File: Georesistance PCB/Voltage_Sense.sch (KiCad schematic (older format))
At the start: 26 parts, among them Q1 MMBF4117, Q2 MMBF4117, Q3 MMBF4117, Q4 MMBF4117, U1 RS8554, U2 LTC6915HGN-TRPBF, U3 LM4040DBZ-2.5

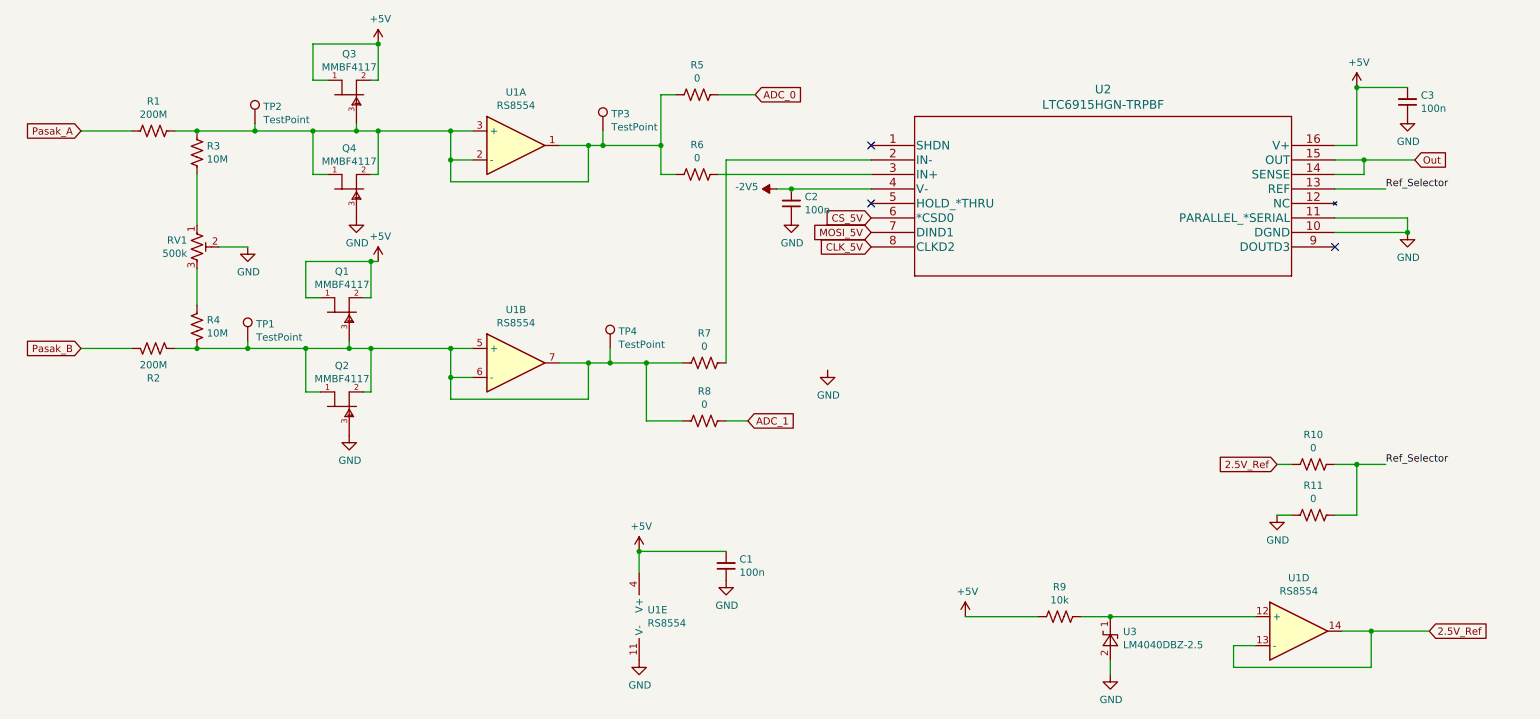
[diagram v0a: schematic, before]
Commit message: Added the PCB layout and simplified schematic
deleted jumper, and fixed misconnection
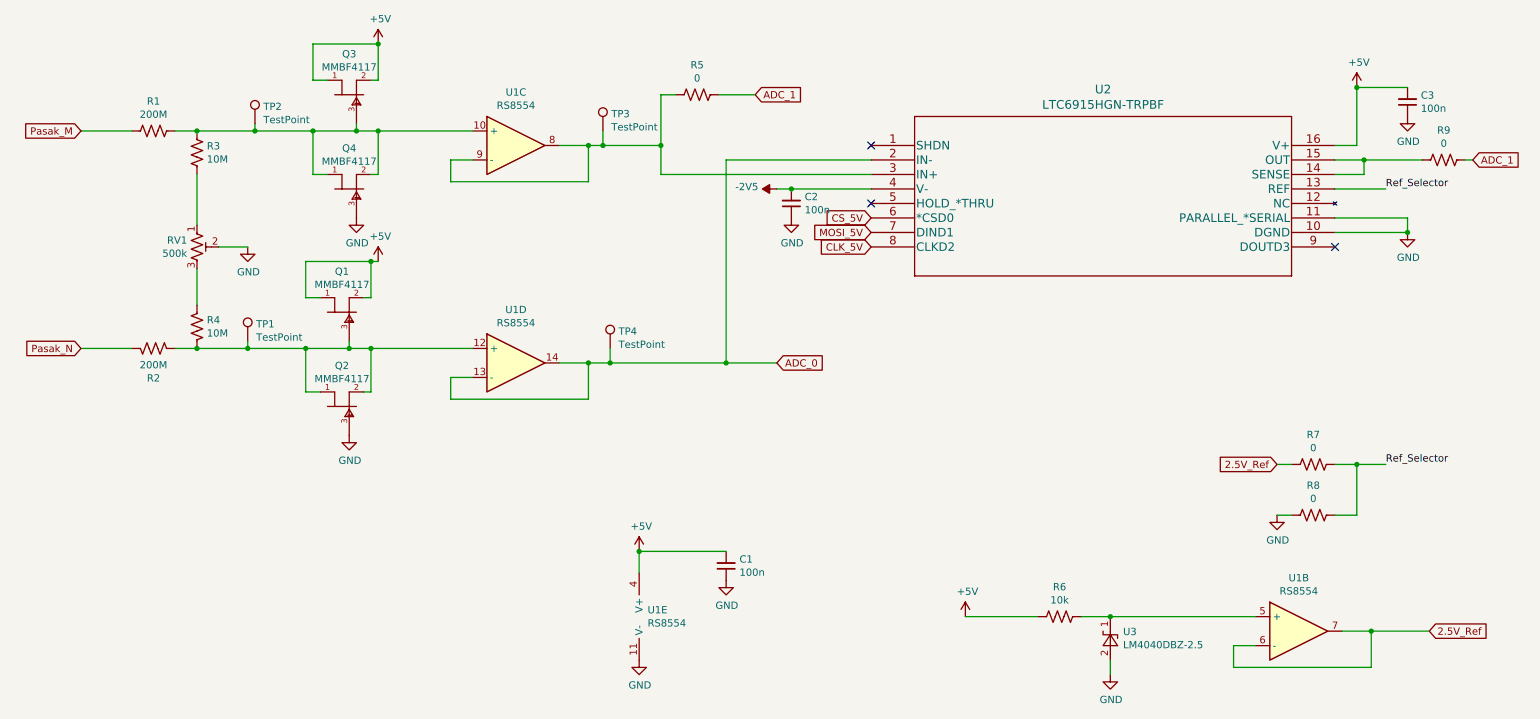
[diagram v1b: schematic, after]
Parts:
- removed R6, R7, R8: 0, Resistor_SMD:R_0402_1005Metric_Pad0.72x0.64mm_HandSolder, symbol Device:R_US
- added R9: 0, Resistor_SMD:R_0402_1005Metric_Pad0.72x0.64mm_HandSolder, symbol Device:R_US
- TP1, TP2, TP3, TP4: footprint TestPoint:TestPoint_Loop_D2.54mm_Drill1.5mm_Beaded -> TestPoint:TestPoint_THTPad_D1.0mm_Drill0.5mm
- renumbered R9 to R6, R10 to R7, R11 to R8
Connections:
- net 2.5V_Ref: now also U1.6 (-), U1.7; no longer U1.13 (-), U1.14
- net ADC_0: now also TP4.1, U1.13 (-), U1.14, U2.2 (IN-); no longer R5.1
- net ADC_1: now also R5.1, R9.1
- net at Q3.3 (G), Q4.1 (D), Q4.2 (S)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: now also U1.10 (+); no longer R5.2, TP3.1, U1.1, U1.2 (-), U1.3 (+)
- net at Q1.3 (G), Q2.1 (D), Q2.2 (S)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: now also U1.12 (+); no longer TP4.1, U1.5 (+), U1.6 (-), U1.7
- net at U2.3 (IN+): now also R5.2, TP3.1, U1.8, U1.9 (-)
- net at R6.1, U3.1 (K): now also U1.5 (+); no longer U1.12 (+)
- net Out: no longer names the net of U2.14 (SENSE), U2.15 (OUT)
- net Out: now also R9.2
- net Pasak_A renamed Pasak_M
- net Pasak_B renamed Pasak_N
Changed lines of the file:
@@
 F 0 "TP2" H 2458 2018 50  0000 L CNN
 F 1 "TestPoint" H 2458 1927 50  0000 L CNN
-F 2 "TestPoint:TestPoint_Loop_D2.54mm_Drill1.5mm_Beaded" H 2600 1900 50  0001 C CNN
+F 2 "TestPoint:TestPoint_THTPad_D1.0mm_Drill0.5mm" H 2600 1900 50  0001 C CNN
 F 3 "~" H 2600 1900 50  0001 C CNN
 	1    2400 1900
@@
 F 0 "TP1" H 2408 3518 50  0000 L CNN
 F 1 "TestPoint" H 2408 3427 50  0000 L CNN
-F 2 "TestPoint:TestPoint_Loop_D2.54mm_Drill1.5mm_Beaded" H 2550 3400 50  0001 C CNN
+F 2 "TestPoint:TestPoint_THTPad_D1.0mm_Drill0.5mm" H 2550 3400 50  0001 C CNN
 F 3 "~" H 2550 3400 50  0001 C CNN
 	1    2350 3400
@@
 	4700 2050 4700 2300
 Connection ~ 3250 1950
-Connection ~ 3750 2150
 Wire Wire Line
 	3750 2300 3750 2150
@@
 	4700 2300 3750 2300
 Wire Wire Line
-	3750 1950 3250 1950
-Connection ~ 3750 1950
-Wire Wire Line
 	3750 2150 3900 2150
 Wire Wire Line
-	3750 1950 3750 2150
-Wire Wire Line
-	3900 1950 3750 1950
-$Comp
-L Device:Opamp_Quad_Generic U1
-U 1 1 613E6A3C
-P 4200 2050
-F 0 "U1" H 4200 2417 50  0000 C CNN
-F 1 "RS8554" H 4200 2326 50  0000 C CNN
-F 2 "Package_SO:SOIC-14_3.9x8.7mm_P1.27mm" H 4200 2050 50  0001 C CNN
-F 3 "~" H 4200 2050 50  0001 C CNN
-	1    4200 2050
-	1    0    0    -1
-$EndComp
-Wire Wire Line
 	4700 3550 4700 3800
-Connection ~ 3750 3650
 Wire Wire Line
 	4500 3550 4700 3550
@@
 Wire Wire Line
 	4700 3800 3750 3800
-Connection ~ 3750 3450
 Wire Wire Line
 	3750 3650 3900 3650
-Wire Wire Line
-	3750 3450 3750 3650
-Wire Wire Line
-	3900 3450 3750 3450
-Wire Wire Line
-	3200 3450 3750 3450
 Connection ~ 3200 3450
 Wire Wire Line
@@
 	1550 1950 1200 1950
 Text GLabel 1200 1950 0    50   Input ~ 0
-Pasak_A
+Pasak_M
 Text GLabel 1200 3450 0    50   Input ~ 0
-Pasak_B
+Pasak_N
 Wire Wire Line
 	4700 2050 4800 2050
@@
 F 0 "TP3" H 4858 2068 50  0000 L CNN
 F 1 "TestPoint" H 4858 1977 50  0000 L CNN
-F 2 "TestPoint:TestPoint_Loop_D2.54mm_Drill1.5mm_Beaded" H 5000 1950 50  0001 C CNN
+F 2 "TestPoint:TestPoint_THTPad_D1.0mm_Drill0.5mm" H 5000 1950 50  0001 C CNN
 F 3 "~" H 5000 1950 50  0001 C CNN
 	1    4800 1950
@@
 F 0 "TP4" H 4908 3568 50  0000 L CNN
 F 1 "TestPoint" H 4908 3477 50  0000 L CNN
-F 2 "TestPoint:TestPoint_Loop_D2.54mm_Drill1.5mm_Beaded" H 5050 3450 50  0001 C CNN
+F 2 "TestPoint:TestPoint_THTPad_D1.0mm_Drill0.5mm" H 5050 3450 50  0001 C CNN
 F 3 "~" H 5050 3450 50  0001 C CNN
 	1    4850 3450
@@
 	1    0    0    -1
 $EndComp
-Text GLabel 5800 3950 2    50   Input ~ 0
+Text GLabel 6000 3550 2    50   Input ~ 0
+ADC_0
+Text GLabel 5850 1700 2    50   Input ~ 0
 ADC_1
-Text GLabel 5850 1700 2    50   Input ~ 0
-ADC_0
 Wire Wire Line
 	5200 2050 5200 1700
@@
 Connection ~ 5200 2050
 $Comp
-L power:GND #PWR017
+L power:GND #PWR016
 U 1 1 614B48BD
 P 10350 2650
-F 0 "#PWR017" H 10350 2400 50  0001 C CNN
+F 0 "#PWR016" H 10350 2400 50  0001 C CNN
 F 1 "GND" H 10355 2477 50  0000 C CNN
 F 2 "" H 10350 2650 50  0001 C CNN
@@
 	9850 2650 10350 2650
 Wire Wire Line
-	4850 3550 5100 3550
-Wire Wire Line
 	5200 1700 5300 1700
-$Comp
-L power:GND #PWR011
-U 1 1 614BFC8B
-P 6350 3600
-F 0 "#PWR011" H 6350 3350 50  0001 C CNN
-F 1 "GND" H 6355 3427 50  0000 C CNN
-F 2 "" H 6350 3600 50  0001 C CNN
-F 3 "" H 6350 3600 50  0001 C CNN
-	1    6350 3600
-	1    0    0    -1
-$EndComp
 Wire Wire Line
 	9850 2150 10050 2150
@@
 Wire Wire Line
 	10050 2250 9850 2250
-Wire Wire Line
-	10050 2150 10400 2150
-Connection ~ 10050 2150
-Text GLabel 10400 2150 2    50   Input ~ 0
-Out
+Text GLabel 10800 2150 2    50   Input ~ 0
+ADC_1
 Wire Wire Line
 	10350 2550 10350 2650
@@
 Connection ~ 10350 2650
 $Comp
-L power:+5V #PWR015
+L power:+5V #PWR014
 U 1 1 614C8FE1
 P 10000 1650
-F 0 "#PWR015" H 10000 1500 50  0001 C CNN
+F 0 "#PWR014" H 10000 1500 50  0001 C CNN
 F 1 "+5V" H 10015 1823 50  0000 C CNN
 F 2 "" H 10000 1650 50  0001 C CNN
@@
 NoConn ~ 6650 2450
 NoConn ~ 9850 2750
-Wire Wire Line
-	5200 2250 5300 2250
 Text GLabel 6650 2550 0    50   Input ~ 0
 CS_5V
@@
 Text GLabel 6650 2650 0    50   Input ~ 0
 MOSI_5V
-$Comp
-L Device:R_US R7
-U 1 1 6149AF9B
-P 5500 3550
-F 0 "R7" V 5295 3550 50  0000 C CNN
-F 1 "0" V 5386 3550 50  0000 C CNN
-F 2 "Resistor_SMD:R_0402_1005Metric_Pad0.72x0.64mm_HandSolder" V 5540 3540 50  0001 C CNN
-F 3 "~" H 5500 3550 50  0001 C CNN
-	1    5500 3550
-	0    1    1    0
-$EndComp
-$Comp
-L Device:R_US R6
-U 1 1 6149BDBD
-P 5450 2250
-F 0 "R6" V 5245 2250 50  0000 C CNN
-F 1 "0" V 5336 2250 50  0000 C CNN
-F 2 "Resistor_SMD:R_0402_1005Metric_Pad0.72x0.64mm_HandSolder" V 5490 2240 50  0001 C CNN
-F 3 "~" H 5450 2250 50  0001 C CNN
-	1    5450 2250
-	0    1    1    0
-$EndComp
-Wire Wire Line
-	5600 2250 6650 2250
 $Comp
 L Device:R_US R5
@@
 Wire Wire Line
 	5600 1700 5850 1700
-$Comp
-L Device:R_US R8
-U 1 1 6149CB47
-P 5500 3950
-F 0 "R8" V 5295 3950 50  0000 C CNN
-F 1 "0" V 5386 3950 50  0000 C CNN
-F 2 "Resistor_SMD:R_0402_1005Metric_Pad0.72x0.64mm_HandSolder" V 5540 3940 50  0001 C CNN
-F 3 "~" H 5500 3950 50  0001 C CNN
-	1    5500 3950
-	0    1    1    0
-$EndComp
-Wire Wire Line
-	5650 3950 5800 3950
-Wire Wire Line
-	5100 3550 5100 3950
-Wire Wire Line
-	5100 3950 5350 3950
-Connection ~ 5100 3550
-Wire Wire Line
-	5100 3550 5350 3550
 Text Label 10200 2350 0    50   ~ 0
 Ref_Selector
@@
 	9150 5500 9300 5500
 $Comp
-L Device:Opamp_Quad_Generic U1
-U 4 1 61568673
-P 9600 5400
-F 0 "U1" H 9600 5767 50  0000 C CNN
-F 1 "RS8554" H 9600 5676 50  0000 C CNN
-F 2 "Package_SO:SOIC-14_3.9x8.7mm_P1.27mm" H 9600 5400 50  0001 C CNN
-F 3 "~" H 9600 5400 50  0001 C CNN
-	4    9600 5400
-	1    0    0    -1
-$EndComp
-$Comp
-L power:GND #PWR013
+L power:GND #PWR012
 U 1 1 61574509
 P 8300 5700
-F 0 "#PWR013" H 8300 5450 50  0001 C CNN
+F 0 "#PWR012" H 8300 5450 50  0001 C CNN
 F 1 "GND" H 8305 5527 50  0000 C CNN
 F 2 "" H 8300 5700 50  0001 C CNN
@@
 	9300 5300 8300 5300
 $Comp
-L Device:R_US R9
+L Device:R_US R6
 U 1 1 61582168
 P 7950 5300
-F 0 "R9" V 7745 5300 50  0000 C CNN
+F 0 "R6" V 7745 5300 50  0000 C CNN
 F 1 "10k" V 7836 5300 50  0000 C CNN
 F 2 "Resistor_THT:R_Axial_DIN0207_L6.3mm_D2.5mm_P7.62mm_Horizontal" V 7990 5290 50  0001 C CNN
@@
 Connection ~ 8300 5300
 $Comp
-L power:+5V #PWR012
+L power:+5V #PWR011
 U 1 1 61585173
 P 7300 5300
-F 0 "#PWR012" H 7300 5150 50  0001 C CNN
+F 0 "#PWR011" H 7300 5150 50  0001 C CNN
 F 1 "+5V" H 7315 5473 50  0000 C CNN
 F 2 "" H 7300 5300 50  0001 C CNN
@@
 2.5V_Ref
 $Comp
-L power:GND #PWR014
+L power:GND #PWR013
 U 1 1 61591BB5
 P 9450 4600
-F 0 "#PWR014" H 9450 4350 50  0001 C CNN
+F 0 "#PWR013" H 9450 4350 50  0001 C CNN
 F 1 "GND" H 9455 4427 50  0000 C CNN
 F 2 "" H 9450 4600 50  0001 C CNN
@@
 $EndComp
 $Comp
-L Device:R_US R10
+L Device:R_US R7
 U 1 1 61592648
 P 9700 4250
-F 0 "R10" V 9495 4250 50  0000 C CNN
+F 0 "R7" V 9495 4250 50  0000 C CNN
 F 1 "0" V 9586 4250 50  0000 C CNN
 F 2 "Resistor_SMD:R_0402_1005Metric_Pad0.72x0.64mm_HandSolder" V 9740 4240 50  0001 C CNN
@@
 	9550 4250 9450 4250
 $Comp
-L Device:R_US R11
+L Device:R_US R8
 U 1 1 61599A3D
 P 9700 4600
-F 0 "R11" V 9495 4600 50  0000 C CNN
+F 0 "R8" V 9495 4600 50  0000 C CNN
 F 1 "0" V 9586 4600 50  0000 C CNN
 F 2 "Resistor_SMD:R_0402_1005Metric_Pad0.72x0.64mm_HandSolder" V 9740 4590 50  0001 C CNN
@@
 Wire Wire Line
 	10000 4250 10200 4250
-$Comp
-L Device:Opamp_Quad_Generic U1
-U 5 1 615F9915
-P 5150 5300
-F 0 "U1" H 5108 5346 50  0000 L CNN
-F 1 "RS8554" H 5108 5255 50  0000 L CNN
-F 2 "Package_SO:SOIC-14_3.9x8.7mm_P1.27mm" H 5150 5300 50  0001 C CNN
-F 3 "~" H 5150 5300 50  0001 C CNN
-	5    5150 5300
-	1    0    0    -1
-$EndComp
 $Comp
 L power:+5V #PWR06
@@
 $EndComp
 $Comp
-L power:GND #PWR016
+L power:GND #PWR015
 U 1 1 6160913B
 P 10350 1850
-F 0 "#PWR016" H 10350 1600 50  0001 C CNN
+F 0 "#PWR015" H 10350 1600 50  0001 C CNN
 F 1 "GND" H 10355 1677 50  0000 C CNN
 F 2 "" H 10350 1850 50  0001 C CNN
@@
 Connection ~ 6100 2350
 $Comp
+L Device:R_US R9
+U 1 1 618A5C46
+P 10600 2150
+F 0 "R9" V 10395 2150 50  0000 C CNN
+F 1 "0" V 10486 2150 50  0000 C CNN
+F 2 "Resistor_SMD:R_0402_1005Metric_Pad0.72x0.64mm_HandSolder" V 10640 2140 50  0001 C CNN
+F 3 "~" H 10600 2150 50  0001 C CNN
+	1    10600 2150
+	0    1    1    0
+$EndComp
+Wire Wire Line
+	10750 2150 10800 2150
+Wire Wire Line
+	10450 2150 10050 2150
+Connection ~ 10050 2150
+Wire Wire Line
+	4850 3550 5650 3550
+Wire Wire Line
+	5650 3550 6000 3550
+Connection ~ 5650 3550
+Wire Wire Line
+	5200 2250 6650 2250
+Wire Wire Line
+	3250 1950 3900 1950
+Wire Wire Line
+	3200 3450 3900 3450
+$Comp
 L Device:Opamp_Quad_Generic U1
-U 2 1 613E6A4B
+U 3 1 613E6A3C
+P 4200 2050
+F 0 "U1" H 4200 2417 50  0000 C CNN
+F 1 "RS8554" H 4200 2326 50  0000 C CNN
+F 2 "Package_SO:SOIC-14_3.9x8.7mm_P1.27mm" H 4200 2050 50  0001 C CNN
+F 3 "~" H 4200 2050 50  0001 C CNN
+	3    4200 2050
+	1    0    0    -1
+$EndComp
+$Comp
+L Device:Opamp_Quad_Generic U1
+U 5 1 615F9915
+P 5150 5300
+F 0 "U1" H 5108 5346 50  0000 L CNN
+F 1 "RS8554" H 5108 5255 50  0000 L CNN
+F 2 "Package_SO:SOIC-14_3.9x8.7mm_P1.27mm" H 5150 5300 50  0001 C CNN
+F 3 "~" H 5150 5300 50  0001 C CNN
+	5    5150 5300
+	1    0    0    -1
+$EndComp
+$Comp
+L Device:Opamp_Quad_Generic U1
+U 2 1 61568673
+P 9600 5400
+F 0 "U1" H 9600 5767 50  0000 C CNN
+F 1 "RS8554" H 9600 5676 50  0000 C CNN
+F 2 "Package_SO:SOIC-14_3.9x8.7mm_P1.27mm" H 9600 5400 50  0001 C CNN
+F 3 "~" H 9600 5400 50  0001 C CNN
+	2    9600 5400
+	1    0    0    -1
+$EndComp
+$Comp
+L Device:Opamp_Quad_Generic U1
+U 4 1 613E6A4B
 P 4200 3550
 F 0 "U1" H 4200 3917 50  0000 C CNN
@@
 F 2 "Package_SO:SOIC-14_3.9x8.7mm_P1.27mm" H 4200 3550 50  0001 C CNN
 F 3 "~" H 4200 3550 50  0001 C CNN
-	2    4200 3550
-	1    0    0    -1
-$EndComp
+	4    4200 3550
+	1    0    0    -1
+$EndComp

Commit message: added things
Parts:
- RV1: value 500k -> 200k
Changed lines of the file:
@@
 P 2000 2750
 F 0 "RV1" H 1932 2796 50  0000 R CNN
-F 1 "500k" H 1932 2705 50  0000 R CNN
+F 1 "200k" H 1932 2705 50  0000 R CNN
 F 2 "Potentiometer_THT:Potentiometer_ACP_CA9-H5_Horizontal" H 2000 2750 50  0001 C CNN
 F 3 "~" H 2000 2750 50  0001 C CNN
